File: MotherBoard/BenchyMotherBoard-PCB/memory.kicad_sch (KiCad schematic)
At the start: 68 parts, among them U1 STM32MP157FAB1, U11 IS43TR16256B-125KBLI

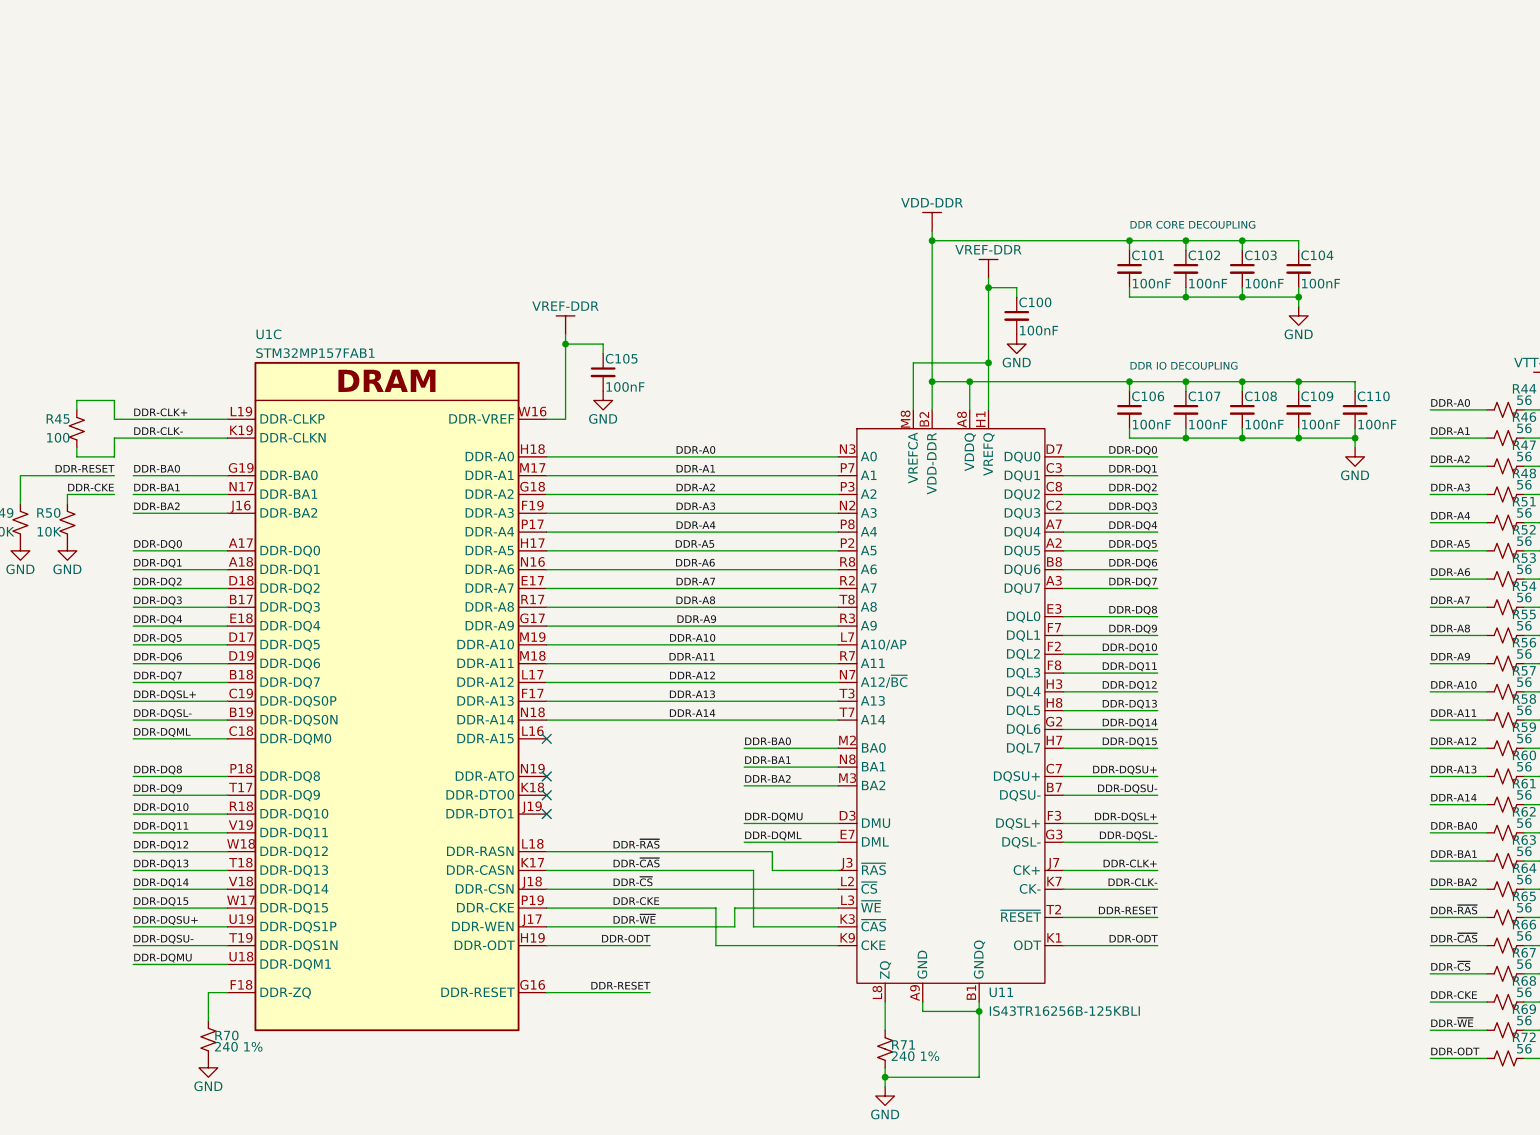
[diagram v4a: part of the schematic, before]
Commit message: Start DDR3 layout
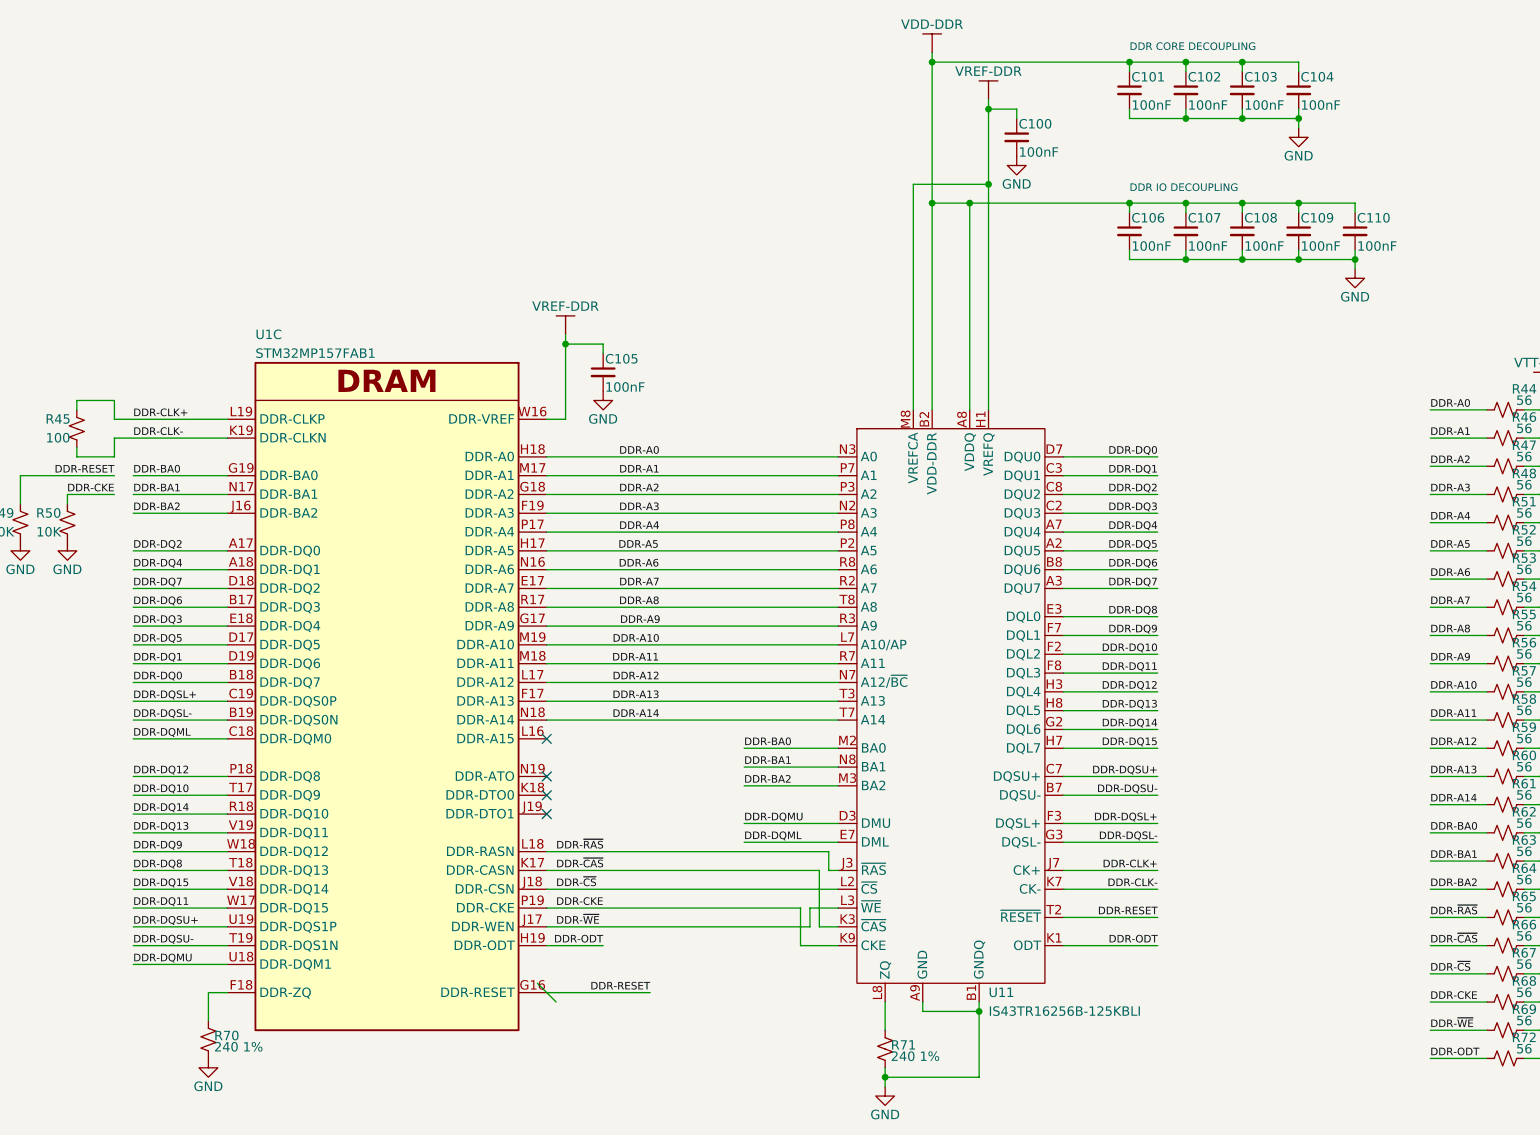
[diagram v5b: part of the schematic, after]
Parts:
- C101, C102, C103, C104, C106, C107, C108, C109, C110: footprint Capacitor_SMD:C_0603_1608Metric -> Capacitor_SMD:C_0402_1005Metric
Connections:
- net DDR-DQ0: now also U1.B18 (DDR-DQ7); no longer U1.A17 (DDR-DQ0)
- net DDR-DQ1: now also U1.D19 (DDR-DQ6); no longer U1.A18 (DDR-DQ1)
- net DDR-DQ10: now also U1.T17 (DDR-DQ9); no longer U1.R18 (DDR-DQ10)
- net DDR-DQ11: now also U1.W17 (DDR-DQ15); no longer U1.V19 (DDR-DQ11)
- net DDR-DQ12: now also U1.P18 (DDR-DQ8); no longer U1.W18 (DDR-DQ12)
- net DDR-DQ13: now also U1.V19 (DDR-DQ11); no longer U1.T18 (DDR-DQ13)
- net DDR-DQ14: now also U1.R18 (DDR-DQ10); no longer U1.V18 (DDR-DQ14)
- net DDR-DQ15: now also U1.V18 (DDR-DQ14); no longer U1.W17 (DDR-DQ15)
- net DDR-DQ2: now also U1.A17 (DDR-DQ0); no longer U1.D18 (DDR-DQ2)
- net DDR-DQ3: now also U1.E18 (DDR-DQ4); no longer U1.B17 (DDR-DQ3)
- net DDR-DQ4: now also U1.A18 (DDR-DQ1); no longer U1.E18 (DDR-DQ4)
- net DDR-DQ6: now also U1.B17 (DDR-DQ3); no longer U1.D19 (DDR-DQ6)
- net DDR-DQ7: now also U1.D18 (DDR-DQ2); no longer U1.B18 (DDR-DQ7)
- net DDR-DQ8: now also U1.T18 (DDR-DQ13); no longer U1.P18 (DDR-DQ8)
- net DDR-DQ9: now also U1.W18 (DDR-DQ12); no longer U1.T17 (DDR-DQ9)
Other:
- moved on the sheet: C100, C101, C102, C103, C104, C106, C107, C108, C109, C110
